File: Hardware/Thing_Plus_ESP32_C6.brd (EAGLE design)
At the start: 22.9 x 58.4 mm, 104 parts, among them J1 THING_PLUS_LOGICAL, J4 QWIIC_RIGHT_ANGLE, J5 MICRO-SDFRICTION, Q1 20V/4.2A/52mΩ/1.4W, U1 ESP32-C6-WROOM-1-NARROW, U2 RT9080-33GJ5, U3 MCP73831, U4 MAX17048

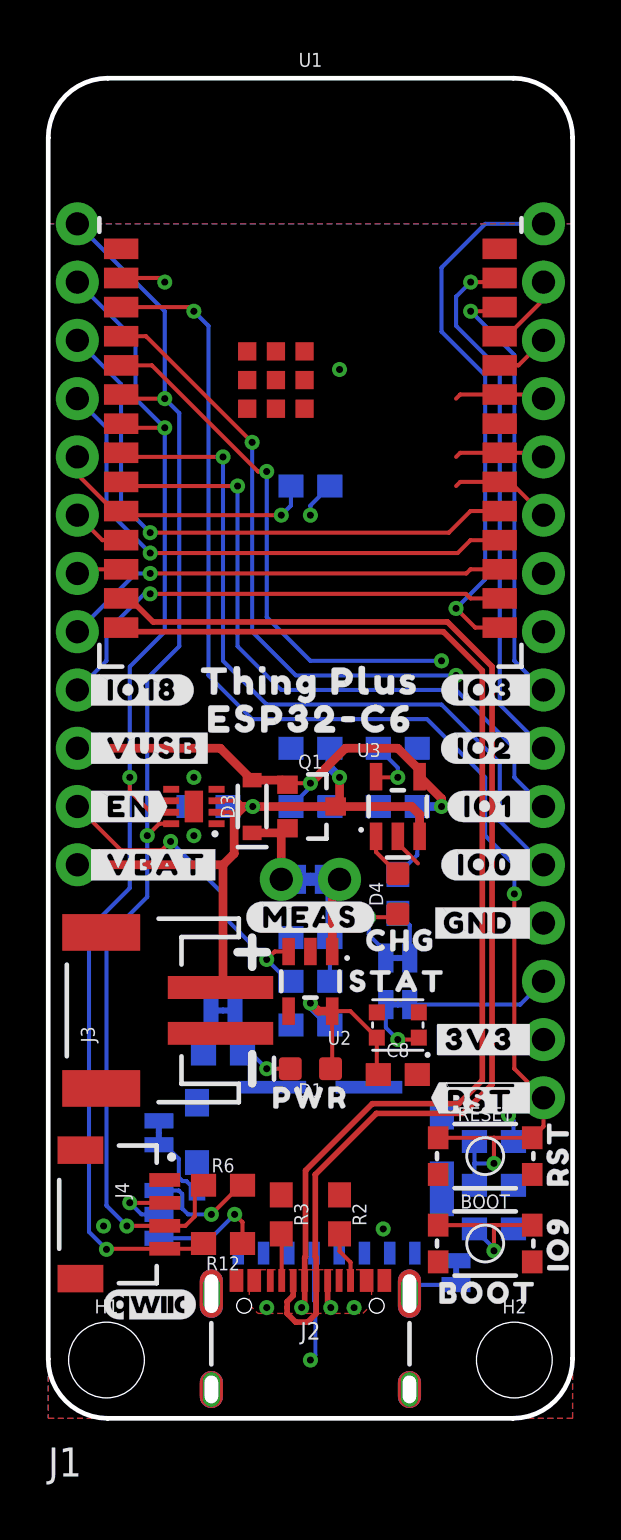
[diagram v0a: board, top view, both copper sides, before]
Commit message: Finish initial schematic and layout
Organized schematic
Rearranged power circuitry to make routing other components easier
Finished routing board
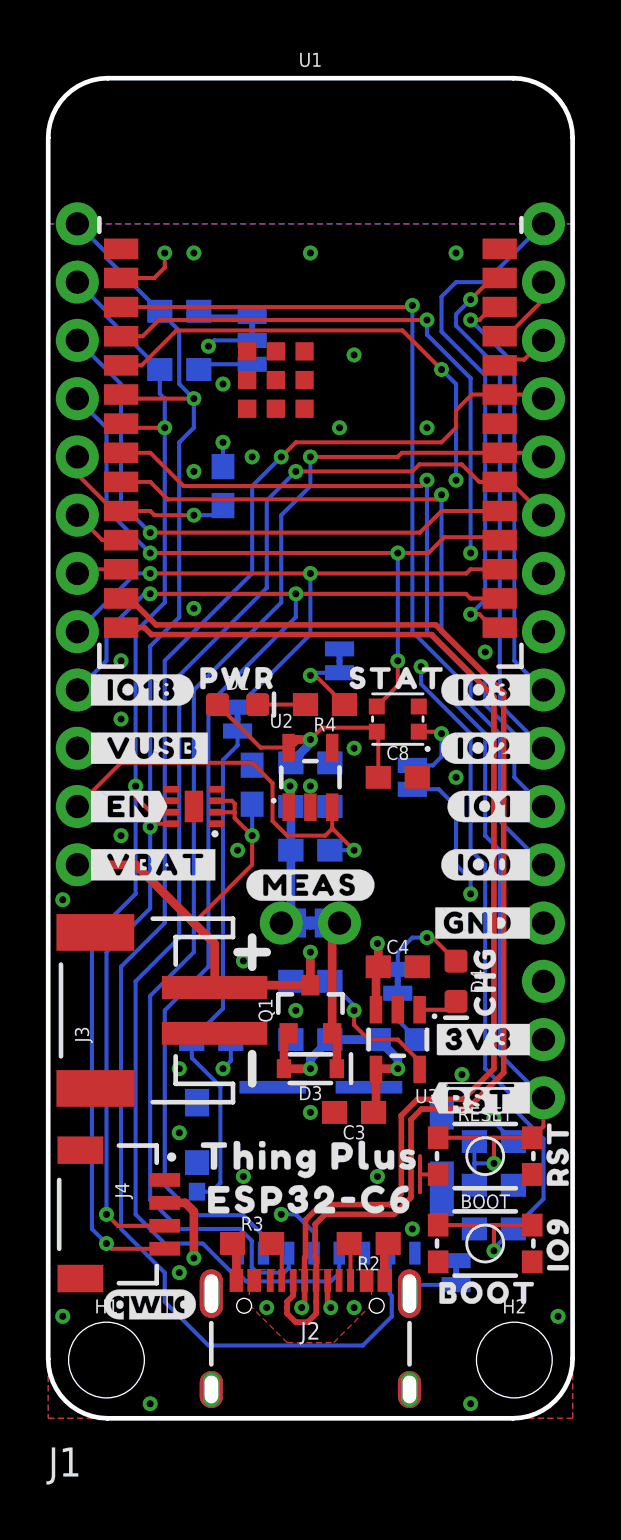
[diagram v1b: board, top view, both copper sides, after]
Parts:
- added R5: 100k, SparkFun-Resistors:0603
- moved U$2 39.6 mm to (9.53, 47.0), turned to 0 degrees
- moved I2C 38.3 mm to (8.89, 47.0)
- moved R12 38.1 mm to (5.71, 45.7), flipped to the bottom, turned to 0 degrees
- moved R6 38.1 mm to (5.71, 48.3), flipped to the bottom, turned to 180 degrees
- moved U$46 21.0 mm to (11.4, 9.53)
- moved U$45 20.7 mm to (11.4, 11.4)
- moved U$53 18.6 mm to (8.26, 32.3)
- moved SD_DET 18.4 mm to (8.26, 30.5)
- moved U$41 17.7 mm to (8.89, 30.5), turned to 0 degrees
- moved D1 16.2 mm to (8.26, 31.1), turned to 0 degrees
- moved PWR 16.1 mm to (12.7, 33.0), turned to 270 degrees
- moved R4 15.9 mm to (12.1, 31.1), flipped to the top
- moved U$52 15.3 mm to (12.1, 33.0), turned to 0 degrees
- moved C3 13.5 mm to (13.3, 13.3), flipped to the top, turned to 180 degrees
- moved D5 13.3 mm to (15.2, 30.5)
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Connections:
- removed net IO18: J1.9, U1.16
- removed net IO19: J1.8, U1.17
- removed net IO20: J1.4, U1.18
- removed net SD_CS: J5.2
- removed net SD_DET: SD_DET.2
- new net IO18/SD_CS: J1.9, J5.2, U1.16
- new net IO19/SD_DET: J1.8, SD_DET.2, U1.17
- new net IO20/STAT: D5.DI, J1.4, U1.18
- net 3.3V: now also R5.2
- net N$3: now also R5.1
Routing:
- net IO15/POCI: track 3.96 -> 67.6 mm, vias 0 -> 1
- net IO18/SD_CS: track 0.00 -> 55.1 mm, vias 0 -> 2
- net IO22/SCK: track 4.49 -> 58.2 mm, vias 0 -> 1
- net IO23/PICO: track 3.96 -> 54.4 mm, vias 0 -> 1
- net IO20/STAT: track 0.00 -> 30.7 mm, vias 0 -> 3
- net IO9/BOOT: track 30.2 -> 59.1 mm, vias 2 -> 3
- net IO19/SD_DET: track 0.00 -> 26.8 mm, vias 0 -> 2
- net IO20: track 23.5 -> 0.00 mm, vias 1 -> 0
- net IO18: track 21.0 -> 0.00 mm, vias 1 -> 0
- net IO19: track 19.5 -> 0.00 mm, vias 1 -> 0
- net N$3: track 2.98 -> 22.2 mm
- net LED_DO: track 6.25 -> 12.9 mm, vias 0 -> 1
- net 3.3V: track 21.6 -> 26.2 mm, vias 6 -> 8
- net GND: track 1.55 -> 5.73 mm, vias 5 -> 33
- net IO8: track 11.8 -> 8.02 mm
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
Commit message: Design review updates
Add measures
Add ordering instructions
Add notes about jumpers
Add voltage regulator parameters
Rearrange LED section in schematic
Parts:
- added U$57: (no value), SparkFun-Aesthetics:ORDERING_INSTRUCTIONS
- moved FRAME1 16.5 mm to (-11.4, -25.4)
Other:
- board text added: "4-layer JLC7628 Stackup Material: TG135-140 1oz outer layers 0.5oz inner layers Board thickness: 1.6mm Soldermask: Red Silkscreen: White Surface Finish: Lead-Free HASL"
- board text added: "Units: Inches"
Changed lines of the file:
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@@
 <drawing>
 <settings>
-<setting alwaysvectorfont="yes"/>
+<setting alwaysvectorfont="no"/>
 <setting verticaltext="up"/>
 </settings>
@@
 <layers>
 <layer number="1" name="Top" color="4" fill="1" visible="yes" active="yes"/>
-<layer number="2" name="Route2" color="23" fill="1" visible="yes" active="yes"/>
-<layer number="15" name="Route15" color="11" fill="1" visible="yes" active="yes"/>
+<layer number="2" name="Route2" color="23" fill="1" visible="no" active="yes"/>
+<layer number="15" name="Route15" color="11" fill="1" visible="no" active="yes"/>
 <layer number="16" name="Bottom" color="1" fill="1" visible="yes" active="yes"/>
 <layer number="17" name="Pads" color="2" fill="1" visible="yes" active="yes"/>
@@
 <wire x1="8.255" y1="20.32" x2="9.525" y2="20.32" width="0.381" layer="21"/>
 <wire x1="8.89" y1="15.875" x2="8.89" y2="14.605" width="0.381" layer="21"/>
-<text x="15.24" y="-8.89" size="1.778" layer="51" font="vector">Dryw Wade</text>
+<text x="15.24" y="-25.4" size="1.778" layer="51" font="vector">Dryw Wade</text>
+<dimension x1="0" y1="0" x2="2.54" y2="0" x3="1.27" y3="-3.81" textsize="1.778" textratio="15" layer="47" unit="inch"/>
+<dimension x1="0" y1="0" x2="11.43" y2="0" x3="5.715" y3="-7.62" textsize="1.778" textratio="15" layer="47" unit="inch"/>
+<dimension x1="0" y1="0" x2="20.32" y2="0" x3="10.16" y3="-11.43" textsize="1.778" textratio="15" layer="47" unit="inch"/>
+<dimension x1="0" y1="0" x2="22.86" y2="0" x3="11.43" y3="-15.24" textsize="1.778" textratio="15" layer="47" unit="inch"/>
+<dimension x1="0" y1="0" x2="0" y2="8.89" x3="-1.27" y3="4.445" textsize="1.778" textratio="15" layer="47" unit="inch"/>
+<dimension x1="0" y1="0" x2="0" y2="17.78" x3="-5.08" y3="8.89" textsize="1.778" textratio="15" layer="47" unit="inch"/>
+<dimension x1="0" y1="0" x2="0" y2="24.13" x3="-8.89" y3="12.065" textsize="1.778" textratio="15" layer="47" unit="inch"/>
+<dimension x1="0" y1="0" x2="0" y2="52.07" x3="-12.7" y3="26.035" textsize="1.778" textratio="15" layer="47" unit="inch"/>
+<dimension x1="22.86" y1="0" x2="22.86" y2="2.54" x3="26.67" y3="1.27" textsize="1.778" textratio="15" layer="47" unit="inch"/>
+<dimension x1="22.86" y1="0" x2="22.86" y2="13.97" x3="30.48" y3="6.985" textsize="1.778" textratio="15" layer="47" unit="inch"/>
+<dimension x1="0" y1="0" x2="0" y2="58.42" x3="-16.51" y3="29.21" textsize="1.778" textratio="15" layer="47" unit="inch"/>
+<text x="-16.51" y="-2.54" size="1.778" layer="47" font="vector" ratio="15">Units: Inches</text>
+<text x="35.56" y="40.64" size="1.778" layer="51" font="vector" align="top-left">4-layer
+JLC7628 Stackup
+Material: TG135-140
+1oz outer layers
+0.5oz inner layers
+Board thickness: 1.6mm
+Soldermask: Red
+Silkscreen: White
+Surface Finish: Lead-Free HASL</text>
 </plain>
 <attributes>
@@
 </autorouter>
 <elements>
-<element name="FRAME1" library="SparkFun-Aesthetics" package="CREATIVE_COMMONS" value="FRAME-LETTER" x="-11.43" y="-8.89" smashed="yes">
-<attribute name="DESIGNER" value="Dryw Wade" x="-11.43" y="-8.89" size="1.778" layer="27" font="vector" ratio="15" display="off"/>
-<attribute name="REV" value="v01" x="-11.43" y="-8.89" size="1.778" layer="27" font="vector" ratio="15" display="off"/>
+<element name="FRAME1" library="SparkFun-Aesthetics" package="CREATIVE_COMMONS" value="FRAME-LETTER" x="-11.43" y="-25.4" smashed="yes">
+<attribute name="DESIGNER" value="Dryw Wade" x="-11.43" y="-25.4" size="1.778" layer="27" font="vector" ratio="15" display="off"/>
+<attribute name="REV" value="v01" x="-11.43" y="-25.4" size="1.778" layer="27" font="vector" ratio="15" display="off"/>
 </element>
 <element name="U1" library="ESP32-C6-WROOM-1" package="ESP32-C6-WROOM-1-NARROW" value="ESP32-C6-WROOM-1-NARROW" x="11.43" y="45.72" smashed="yes">
@@
 <attribute name="VALUE" x="7.1755" y="17.272" size="0.6096" layer="28" font="vector" ratio="20" rot="MR180" align="top-center"/>
 </element>
+<element name="U$57" library="SparkFun-Aesthetics" package="ORDERING_INSTRUCTIONS" value="" x="34.29" y="50.8" smashed="yes"/>
 </elements>
 <signals>
@@
 </drawing>
 <compatibility>
+<note version="6.3" minversion="6.2.2" severity="warning">
+Since Version 6.2.2 text objects can contain more than one line,
+which will not be processed correctly with this version.
+</note>
 <note version="8.3" severity="warning">
 Since Version 8.3, EAGLE supports URNs for individual library

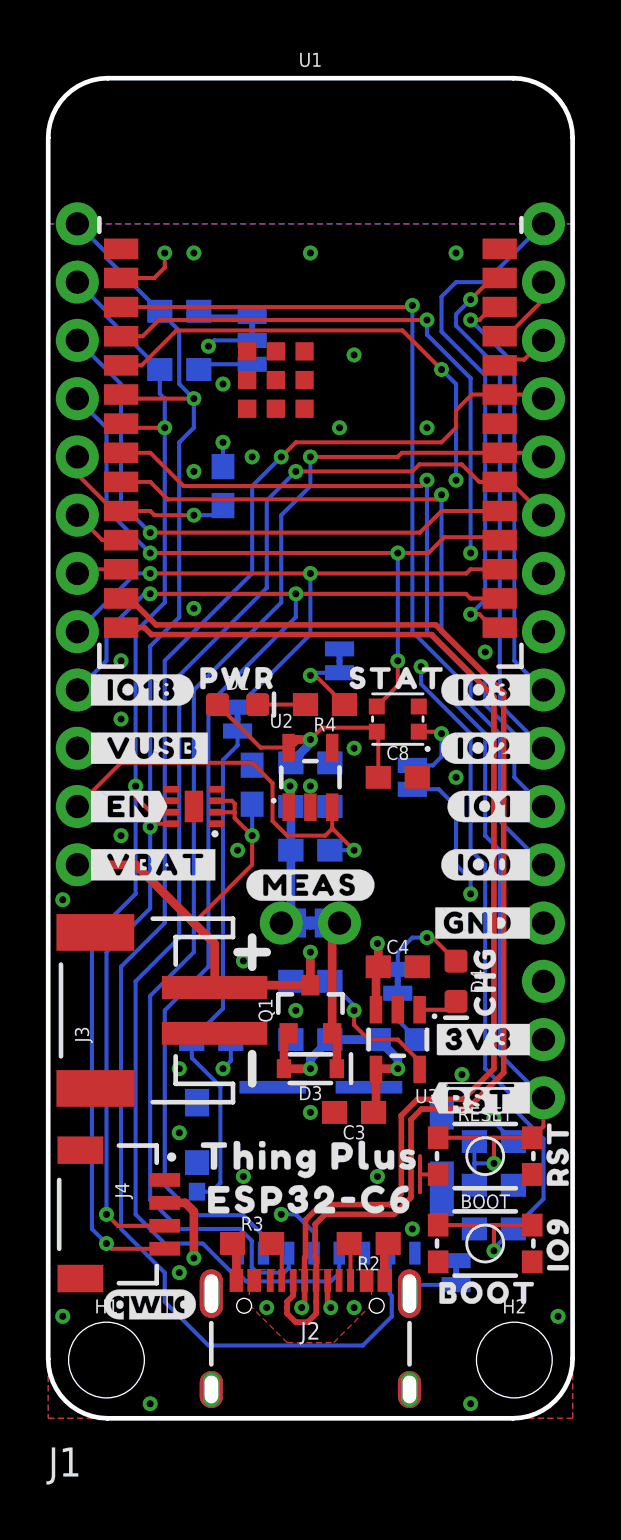
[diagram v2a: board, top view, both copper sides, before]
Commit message: Design review updates
Add RGB label to NC pin
Move CHG LED to make room for RGB label
Optimize GND pours
Add GND vias
Fix acid traps
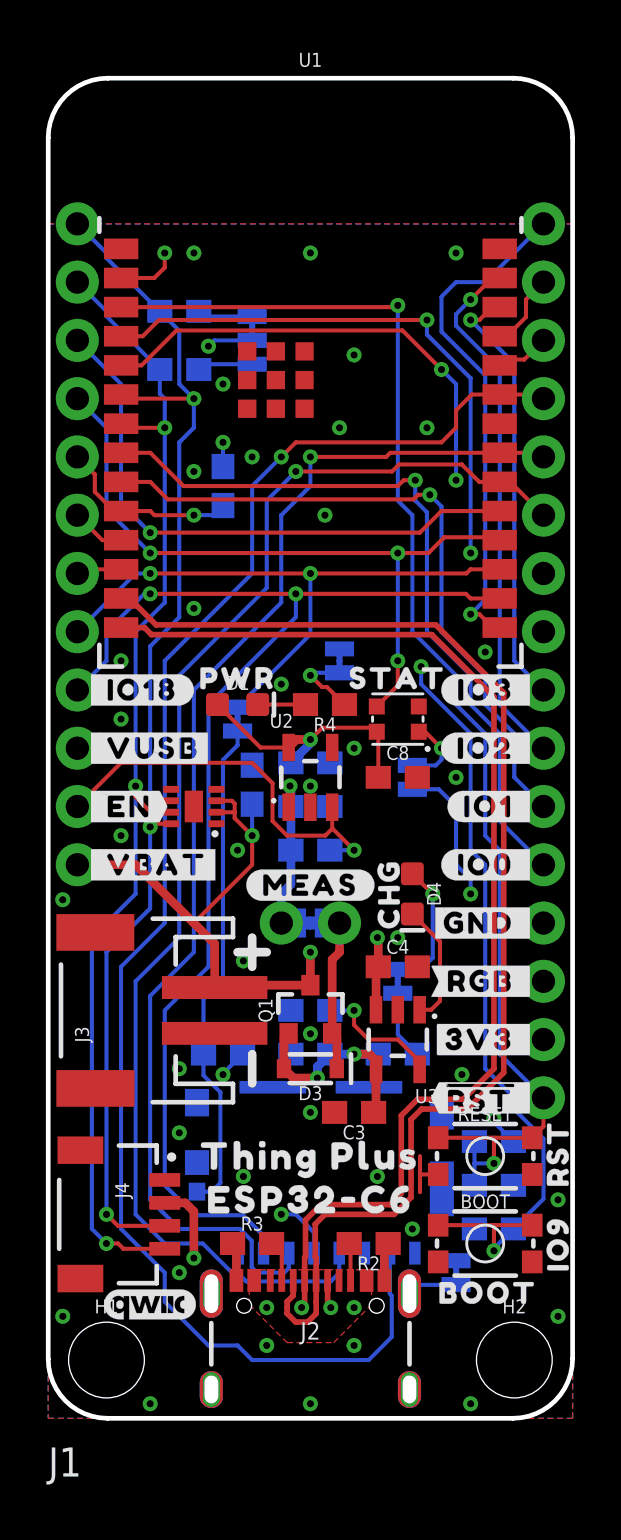
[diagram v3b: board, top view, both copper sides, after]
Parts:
- added U$58: (no value), output:#RGB_#0
- added U$59: (no value), output:#_RGB#0
- moved U$54 5.66 mm to (14.9, 22.9)
- moved D4 4.26 mm to (15.9, 22.9)
- moved R10 1.27 mm to (11.4, 17.8)
- moved U$51 1.27 mm to (14.6, 19.1)
- moved R5 0.81 mm to (7.62, 15.9)
- moved R7 0.64 mm to (11.4, 15.9)
- moved R9 0.64 mm to (15.2, 15.9)
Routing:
- net N$10: track 1.74 -> 5.34 mm
- net N$11: track 3.98 -> 5.77 mm
- net IO15/POCI: track 67.6 -> 68.6 mm
- net N$13: track 6.20 -> 5.55 mm
- net N$12: track 2.37 -> 3.01 mm
- net GND: vias 33 -> 40
